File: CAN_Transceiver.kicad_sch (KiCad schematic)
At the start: 8 parts, among them SW2 SW_DIP_x01, U5 TJA1051T/3/1J

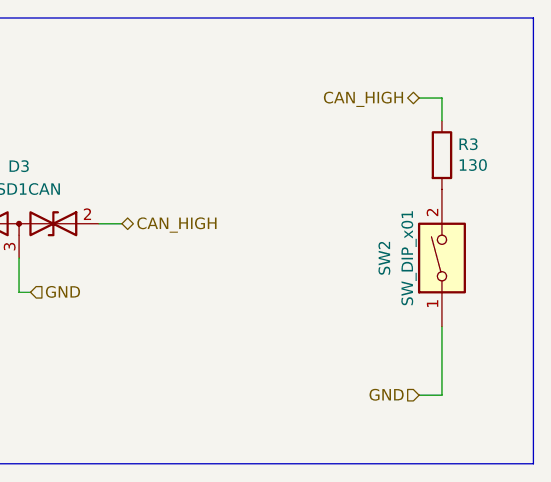
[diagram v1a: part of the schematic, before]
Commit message: Updated Isolated CANTX
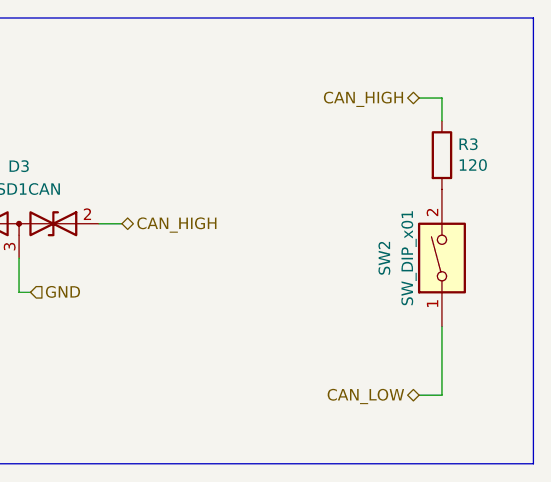
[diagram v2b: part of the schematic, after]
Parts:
- R3: value 130 -> 120
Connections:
- net CAN_LOW: now also SW2.1
- net GND: no longer SW2.1
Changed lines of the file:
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@@
 	(hierarchical_label "GND"
 		(shape input)
+		(at 115.57 93.98 0)
+		(effects
+			(font
+				(size 1.27 1.27)
+			)
+			(justify left)
+		)
+	)
+	(hierarchical_label "CAN_LOW"
+		(shape bidirectional)
 		(at 207.01 100.33 180)
 		(effects
@@
 			)
 			(justify right)
-		)
-	)
-	(hierarchical_label "GND"
-		(shape input)
-		(at 115.57 93.98 0)
-		(effects
-			(font
-				(size 1.27 1.27)
-			)
-			(justify left)
 		)
 	)
@@
 			)
 		)
-		(property "Value" "130"
+		(property "Value" "120"
 			(at 211.328 74.803 0)
 			(effects

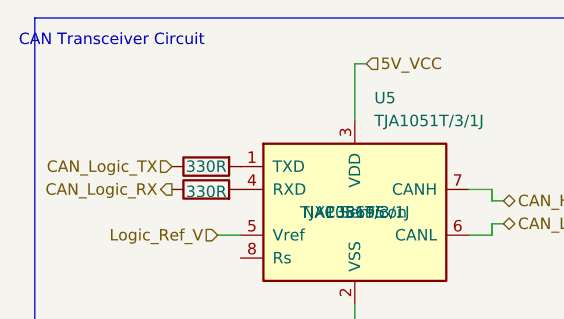
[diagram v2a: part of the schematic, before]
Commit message: Connectors, high side circuits added, layout progressed
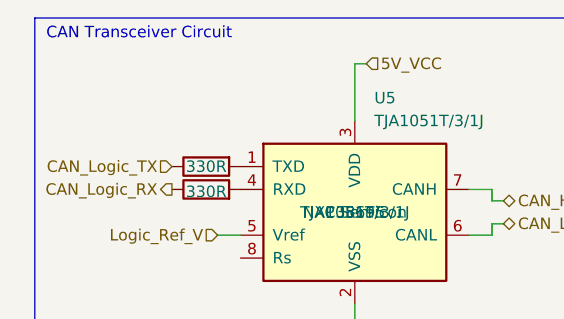
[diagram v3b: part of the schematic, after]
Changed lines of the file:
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@@
 	(text "CAN Transceiver Circuit"
 		(exclude_from_sim no)
-		(at 75.692 61.722 0)
+		(at 78.74 60.96 0)
 		(effects
 			(font
@@
 		(on_board yes)
 		(dnp no)
-		(fields_autoplaced yes)
 		(property "Reference" "U5"
 			(at 115.1909 67.31 0)
@@
 			(project ""
 				(path "/d7e219ab-f530-45f5-8a23-0e6b6d2e3e0f/cdaff6ef-6933-443e-a2a0-6e49d77f85e1"
-					(reference "U7")
+					(reference "U10")
 					(unit 1)
 				)

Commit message: Finalised RS485 Circuit, Layout improvemnts, mounting holes, silkscreen...
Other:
- company: (none) -> eChook
- title: (none) -> BMS Comms Master Board
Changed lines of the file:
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@@
 	(generator_version "9.0")
 	(paper "A4")
+	(title_block
+		(title "BMS Comms Master Board")
+		(date "2025-05-21")
+		(rev "0.1")
+		(company "eChook")
+	)
 	(text "CAN Transceiver Circuit"
 		(exclude_from_sim no)

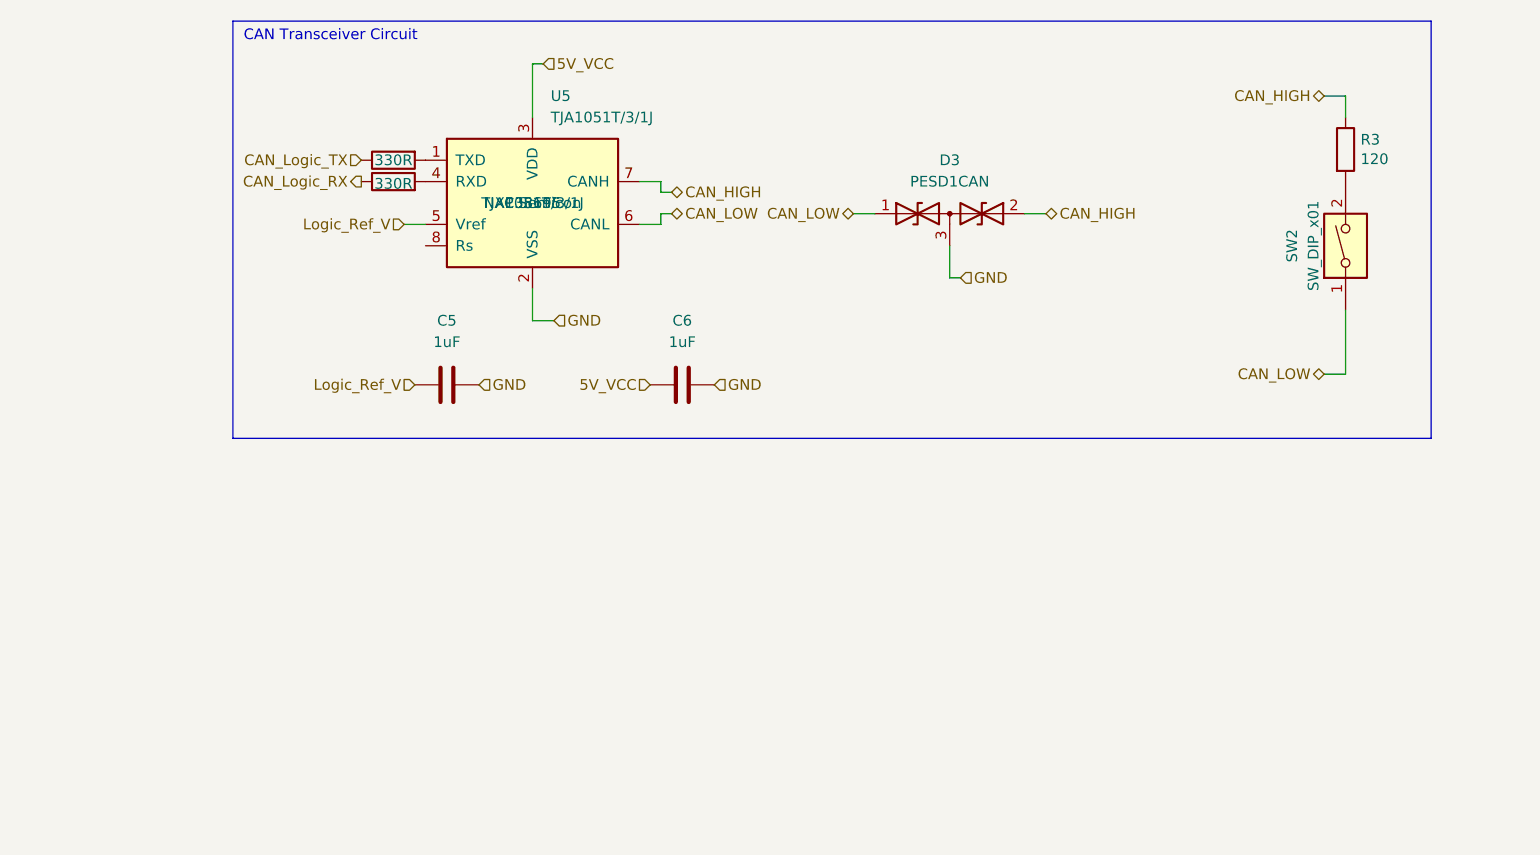
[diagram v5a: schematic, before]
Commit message: J5 Bottom Silkscreen, Schematic organise
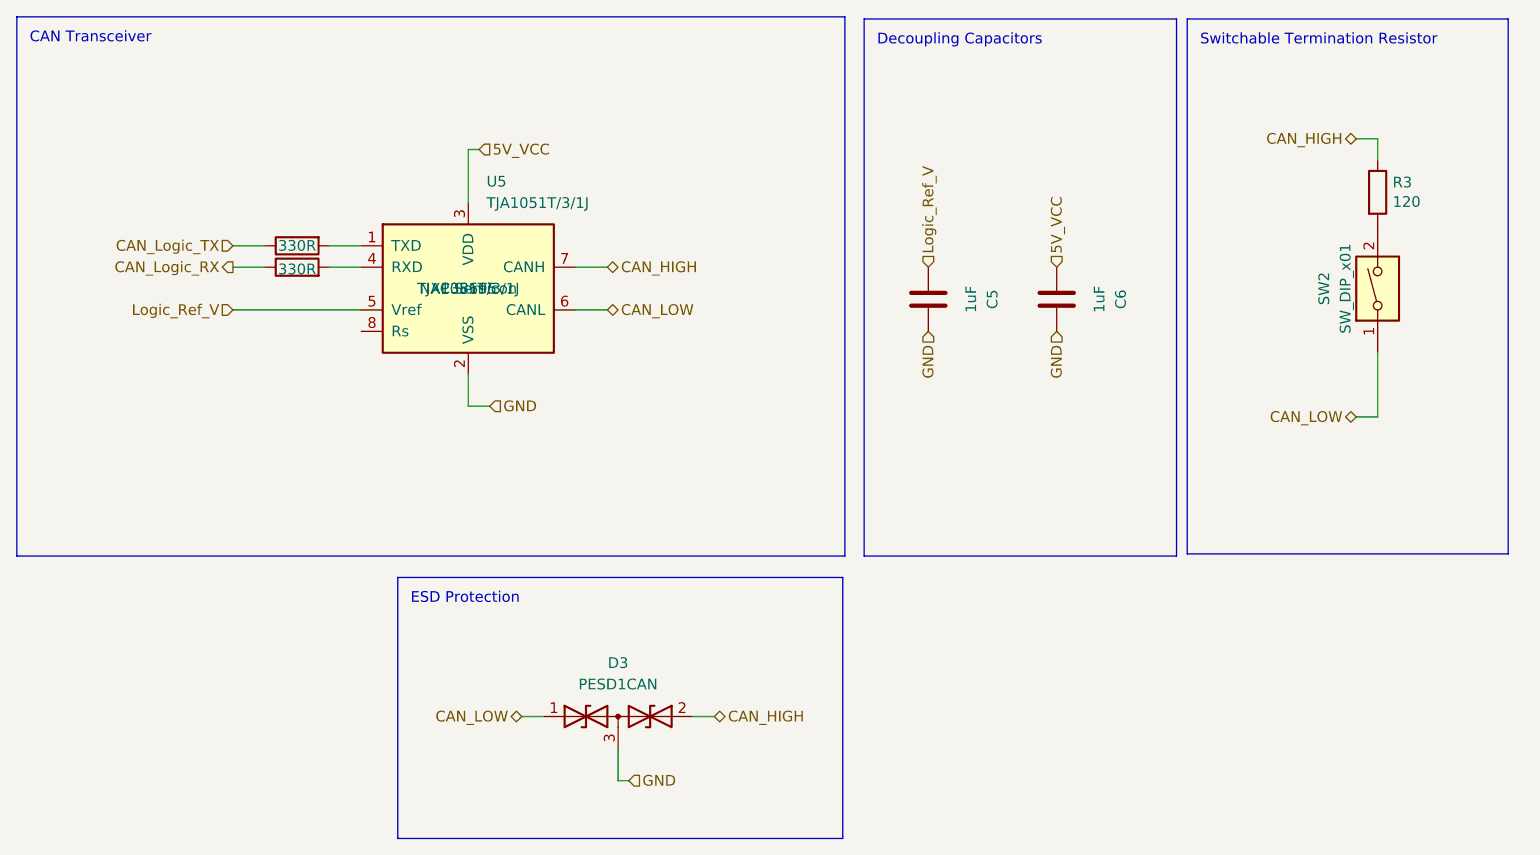
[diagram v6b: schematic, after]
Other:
- note added: "CAN Transceiver"
- note added: "Decoupling Capacitors"
- note added: "ESD Protection"
- note added: "Switchable Termination Resistor"
- note removed: "CAN Transceiver Circuit"
- moved on the sheet: C5, C6, D3, R3, SW2, U5

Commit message: Implemented schematic review suggestions (Notes.txt)
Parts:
- R3: footprint Resistor_SMD:R_0603_1608Metric -> Resistor_SMD:R_0805_2012Metric; LCSC (none) -> C543533
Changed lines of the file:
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@@
 			)
 		)
-		(property "Footprint" "Resistor_SMD:R_0603_1608Metric"
+		(property "Footprint" "Resistor_SMD:R_0805_2012Metric"
 			(at 211.582 78.74 90)
 			(effects
@@
 			)
 		)
-		(property "Description" ""
+		(property "Description" "CAN Termination Resistor 1/2W"
 			(at 213.36 78.74 0)
 			(effects
@@
 			)
 		)
-		(property "LCSC" ""
+		(property "LCSC" "C543533"
 			(at 213.36 78.74 0)
 			(effects
@@
 			)
 		)
-		(property "Datasheet" "~"
+		(property "Datasheet" "https://lcsc.com/datasheet/lcsc_datasheet_2411201840_DEALON-SP-01P_C5160893.pdf"
 			(at 213.36 90.17 0)
 			(effects
